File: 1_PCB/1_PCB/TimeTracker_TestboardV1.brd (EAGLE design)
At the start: 102.5 x 80 mm, 24 parts, among them IC1 7805DT, IC2 7805DT, J1 2908-05WB-MG, U1 WS2812B, U2 WS2812B, U3 WS2812B, U4 WS2812B, U5 SMTM1225, Y1 FX135A-327

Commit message: Humidity and Temp Sensor
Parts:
- added C5: (no value), rcl:C0805
- added HM1: SI7021-A20, SamacSys_Parts:SON100P300X300X80-7N
- added R1, R2: 10k, rcl:R0805
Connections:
- new net EP: HM1.7
- new net N$18: HM1.6, R2.1
- new net SDA: HM1.1, R1.1
- net 3V3: now also C5.1, HM1.5, R1.2, R2.2
- net GND: now also C5.2, HM1.2
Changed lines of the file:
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@@
 <attribute name="VALUE" x="-5.426" y="-20.147" size="1.27" layer="27" align="center"/>
+</element>
+<element name="HM1" library="SamacSys_Parts" package="SON100P300X300X80-7N" value="SI7021-A20" x="77.47" y="6.35" smashed="yes">
+<attribute name="DESCRIPTION" value="I2C HUMIDITY AND TEMPERATURE SENSOR" x="77.47" y="6.35" size="1.778" layer="27" display="off"/>
+<attribute name="HEIGHT" value="0.8mm" x="77.47" y="6.35" size="1.778" layer="27" display="off"/>
+<attribute name="MANUFACTURER_NAME" value="Silicon Labs" x="77.47" y="6.35" size="1.778" layer="27" display="off"/>
+<attribute name="MANUFACTURER_PART_NUMBER" value="Si7021-A20" x="77.47" y="6.35" size="1.778" layer="27" display="off"/>
+<attribute name="MOUSER_PART_NUMBER" value="" x="77.47" y="6.35" size="1.778" layer="27" display="off"/>
+<attribute name="MOUSER_PRICE-STOCK" value="" x="77.47" y="6.35" size="1.778" layer="27" display="off"/>
+<attribute name="NAME" x="88.9" y="3.81" size="1.27" layer="25" align="center"/>
+<attribute name="RS_PART_NUMBER" value="" x="77.47" y="6.35" size="1.778" layer="27" display="off"/>
+<attribute name="RS_PRICE-STOCK" value="" x="77.47" y="6.35" size="1.778" layer="27" display="off"/>
+<attribute name="VALUE" x="90.17" y="5.08" size="1.27" layer="27" align="center"/>
+</element>
+<element name="C5" library="rcl" library_urn="urn:adsk.eagle:library:334" package="C0805" package3d_urn="urn:adsk.eagle:package:23617/2" value="" x="-13.97" y="-33.02" smashed="yes">
+<attribute name="NAME" x="-15.24" y="-31.75" size="1.27" layer="25"/>
+<attribute name="SPICEPREFIX" value="C" x="-13.97" y="-33.02" size="1.778" layer="27" display="off"/>
+<attribute name="VALUE" x="-15.24" y="-35.56" size="1.27" layer="27"/>
+</element>
+<element name="R1" library="rcl" library_urn="urn:adsk.eagle:library:334" package="R0805" package3d_urn="urn:adsk.eagle:package:23553/2" value="10k" x="-13.97" y="-38.1" smashed="yes">
+<attribute name="NAME" x="-14.605" y="-36.83" size="1.27" layer="25"/>
+<attribute name="SPICEPREFIX" value="R" x="-13.97" y="-38.1" size="1.778" layer="27" display="off"/>
+<attribute name="VALUE" x="-14.605" y="-40.64" size="1.27" layer="27"/>
+</element>
+<element name="R2" library="rcl" library_urn="urn:adsk.eagle:library:334" package="R0805" package3d_urn="urn:adsk.eagle:package:23553/2" value="10k" x="-13.97" y="-44.45" smashed="yes">
+<attribute name="NAME" x="-14.605" y="-43.18" size="1.27" layer="25"/>
+<attribute name="SPICEPREFIX" value="R" x="-13.97" y="-44.45" size="1.778" layer="27" display="off"/>
+<attribute name="VALUE" x="-14.605" y="-46.99" size="1.27" layer="27"/>
 </element>
 </elements>
@@
 <contactref element="J1" pad="4"/>
 <contactref element="U$2" pad="8"/>
+<contactref element="HM1" pad="5"/>
+<contactref element="C5" pad="1"/>
+<contactref element="R1" pad="2"/>
+<contactref element="R2" pad="2"/>
 <wire x1="25.14" y1="67.59" x2="72.39" y2="69.85" width="0" layer="19" extent="1-1"/>
 <wire x1="25.4" y1="64.45" x2="25.14" y2="67.59" width="0" layer="19" extent="1-1"/>
 <wire x1="23.7" y1="50.505" x2="25.4" y2="64.45" width="0" layer="19" extent="1-1"/>
 <wire x1="10.92" y1="32.93" x2="23.7" y2="50.505" width="0" layer="19" extent="1-1"/>
+<wire x1="78.92" y1="6.35" x2="72.39" y2="69.85" width="0" layer="19" extent="1-1"/>
+<wire x1="-14.92" y1="-33.02" x2="10.92" y2="32.93" width="0" layer="19" extent="1-1"/>
+<wire x1="-13.02" y1="-38.1" x2="-14.92" y2="-33.02" width="0" layer="19" extent="1-1"/>
+<wire x1="-13.02" y1="-44.45" x2="-13.02" y2="-38.1" width="0" layer="19" extent="1-1"/>
 </signal>
 <signal name="GND">
@@
 <contactref element="LED_12V1" pad="C"/>
 <contactref element="U5" pad="2"/>
+<contactref element="HM1" pad="2"/>
+<contactref element="C5" pad="2"/>
 <wire x1="54.61" y1="29.21" x2="77.47" y2="69.85" width="0" layer="19" extent="1-1"/>
 <wire x1="39.37" y1="24.13" x2="54.61" y2="29.21" width="0" layer="19" extent="1-1"/>
@@
 <wire x1="22.86" y1="74.89" x2="20.574" y2="63.439" width="0" layer="19" extent="1-1"/>
 <wire x1="-5.08" y1="-20.32" x2="26.633" y2="9.22" width="0" layer="19" extent="1-1"/>
+<wire x1="76.02" y1="6.35" x2="-5.08" y2="-20.32" width="0" layer="19" extent="1-1"/>
+<wire x1="-13.02" y1="-33.02" x2="76.02" y2="6.35" width="0" layer="19" extent="1-1"/>
 </signal>
 <signal name="RFIDRESET">
@@
 <wire x1="-13.13" y1="-20.32" x2="19.48" y2="49.205" width="0" layer="19" extent="1-1"/>
 </signal>
+<signal name="EP">
+<contactref element="HM1" pad="7"/>
+</signal>
+<signal name="SDA">
+<contactref element="HM1" pad="1"/>
+<contactref element="R1" pad="1"/>
+<wire x1="-14.92" y1="-38.1" x2="76.02" y2="7.35" width="0" layer="19" extent="1-1"/>
+</signal>
+<signal name="N$18">
+<contactref element="HM1" pad="6"/>
+<contactref element="R2" pad="1"/>
+<wire x1="-14.92" y1="-44.45" x2="78.92" y2="7.35" width="0" layer="19" extent="1-1"/>
+</signal>
 </signals>

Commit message: Nico addition and modifications
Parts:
- removed J1: 2908-05WB-MG, 2908-05WB-MG:3M_2908-05WB-MG
- added JP6: USD_CONNECTOR, SparkFun-Connectors:MICRO-SD-SOCKET-PP
- added R6, R7, R8, R9: 100k, rcl:R0805
- moved U5 105.1 mm to (44.5, 72.4)
- moved Y1 99.9 mm to (55.9, 62.2), turned to 180 degrees
- moved U$2 39.8 mm to (57.1, 67.3), turned to 90 degrees
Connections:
- removed net N$4: J1.8
- removed net N$6: J1.1
- removed net N$7: J1.2
- removed net N$8: J1.3
- new net !CS_3V3: JP6.CS, R9.1
- new net CD: JP6.CD2
- new net CDSDSD: JP6.CD1, R8.1
- new net RSV@1: JP6.RSV1, R6.1
- new net RSV@2: JP6.RSV2, R7.1
- net 3V3: now also JP6.VCC, R6.2, R7.2, R9.2; no longer J1.4
- net 5V: now also R8.2
- net GND: now also JP6.GND, JP6.GND1, JP6.GND3; no longer J1.6
- net N$16: now also U5.3
- net SPIMISO: now also JP6.DO
- net SPIMOSI: now also JP6.DI; no longer J1.7
- net SPISCK: now also JP6.SCLK; no longer J1.5
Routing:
- net N$16: track 0.00 -> 36.6 mm
- net N$14: track 0.00 -> 3.61 mm
- net N$15: track 0.00 -> 3.10 mm

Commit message: Nico
Update PCB
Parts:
- added C6: 0.1uF, SparkFun-Capacitors:0603-CAP
- added C7, C9: 0.1u, rcl:C0805
- added C8: (no value), rcl:C0805
- added R10, R11, R12, R13, R4, R5: 10K, rcl:R0805
- added SJ4, SJ5: (no value), SparkFun-Passives:PAD-JUMPER-3-2OF3_NC_BY_TRACE_YES_SILK_FULL_BOX
- added U6: SX1509, SparkFun-DigitalIC:QFN-28
- moved R8 155.7 mm to (1.58, 19.8), turned to 180 degrees
- moved R7 132.9 mm to (1.71, 9.65), turned to 180 degrees
- moved R2 125.6 mm to (96.5, 15.2)
- moved C5 119.1 mm to (96.5, 11.4)
- moved R6 112.6 mm to (1.71, 2.03), turned to 180 degrees
- moved R1 111.3 mm to (86.4, 10.2), turned to 270 degrees
- moved R9 103.8 mm to (1.71, 5.97), turned to 180 degrees
- moved HM1 15.5 mm to (92.7, 8.89)
- moved JP5 14.8 mm to (30.5, 31.8)
- moved C2 0.92 mm to (25.1, 64.4)
- moved C4 0.28 mm to (7.87, 66.2)
- renumbered IC1 to LD1117DT33TR
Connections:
- removed net !CS_3V3: JP6.CS, R9.1
- removed net CD: JP6.CD2
- removed net N$18: HM1.6, R2.1
- removed net RFIDCS: JP1.1, JP3.2
- removed net RFIDRESET: JP1.7, JP2.2
- removed net SDA: HM1.1, R1.1
- new net !INT: R10.1, U6.9
- new net !RESET: R4.1, U6.23
- new net !SD_CS: JP6.CS, R9.1, U6.27
- new net 10: U6.15
- new net 11: U6.16
- new net 12: U6.19
- new net 13: U6.20
- new net 14: U6.21
- new net 15: U6.22
- new net 4: U6.5
- new net 5: U6.6
- new net 6: U6.7
- new net 7: U6.8
- new net 8: U6.13
- new net 9: U6.14
- new net ADDR0: SJ4.2, U6.26
- new net ADDR1: SJ5.2, U6.10
- new net I2CSCL: HM1.6, R12.1, R2.1, U$1.A5, U$2.6, U6.25
- new net I2CSDA: HM1.1, R1.1, R13.1, U$1.A4, U$2.5, U6.24
- new net LED_DIN: U$1.D2, U4.4
- new net N$6: R11.1, SJ5.1
- new net N$8: R5.1, SJ4.1
- new net OSCIO: U6.11
- new net RFID_CS: JP1.1, JP3.2, U6.1
- new net RFID_RESET: JP1.7, JP2.2, U6.2
- new net SD_CD: JP6.CD2, U6.28
- net 3V3: now also C6.1, C7.1, C8.1, C9.1, R10.2, R11.2, R12.2, R13.2, R4.2, R5.2, R8.2, U6.12, U6.18, U6.4
- net 5V: no longer R8.2
- net GND: now also C6.2, C7.2, C8.2, C9.2, SJ4.3, SJ5.3, U6.17, U6.29, U6.3
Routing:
- net 3V3: track 0.00 -> 329.3 mm
- net I2CSCL: track 0.00 -> 170.2 mm, vias 0 -> 6
- net I2CSDA: track 0.00 -> 153.6 mm, vias 0 -> 5
- net SPISCK: track 0.00 -> 125.3 mm, vias 0 -> 2
- net SPIMOSI: track 0.00 -> 124.1 mm, vias 0 -> 1
- net SPIMISO: track 0.00 -> 123.5 mm, vias 0 -> 1
- net RFID_RESET: track 0.00 -> 87.7 mm, vias 0 -> 1
- net SD_CD: track 0.00 -> 83.5 mm, vias 0 -> 2
- net RFID_CS: track 0.00 -> 76.2 mm
- net 5V: track 27.0 -> 97.5 mm, vias 2 -> 3
- net LED_DIN: track 0.00 -> 37.9 mm, vias 0 -> 1
- net ADDR1: track 0.00 -> 32.2 mm, vias 0 -> 2
- net N$12: track 2.54 -> 21.3 mm
- net RSV@1: track 0.00 -> 15.3 mm
- net N$1: track 23.9 -> 37.9 mm
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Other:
- outline, holes or cut-outs redrawn

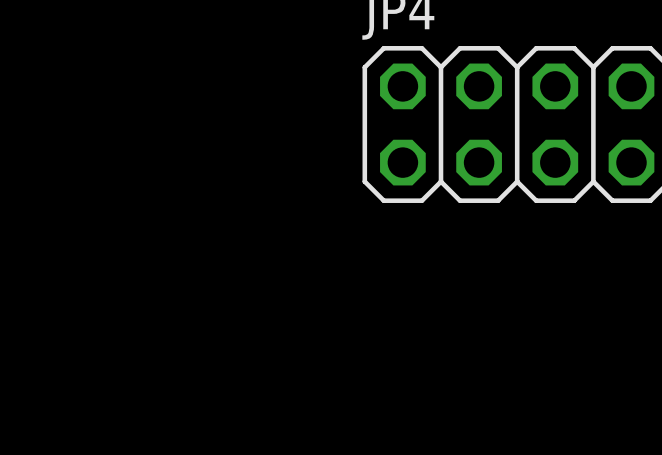
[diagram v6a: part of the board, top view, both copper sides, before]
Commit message: Added a new Voltage Regulator
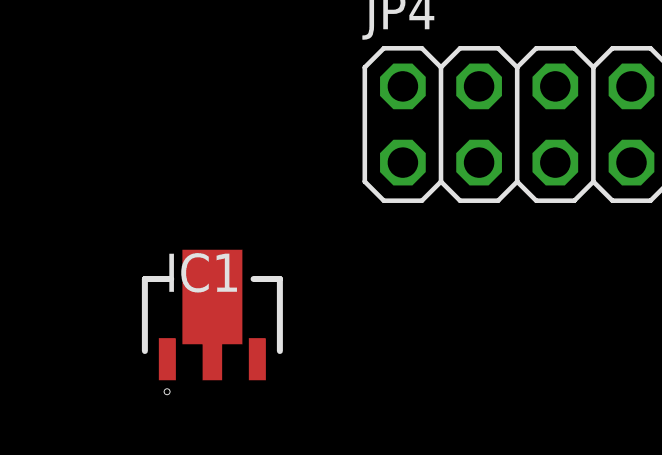
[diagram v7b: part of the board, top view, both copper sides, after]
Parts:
- added IC1: L78L33ABUTR, SamacSys_Parts:ST-SOT-89
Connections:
- new net GND_(TAB): IC1.4
- net GND: now also IC1.2
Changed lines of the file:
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@@
 <?xml version="1.0" encoding="utf-8"?>
 <!DOCTYPE eagle SYSTEM "eagle.dtd">
-<eagle version="9.3.0">
+<eagle version="9.2.2">
 <drawing>
 <settings>
@@
 <attribute name="VALUE" x="57.15" y="73.66" size="1.27" layer="27"/>
 </element>
+<element name="IC1" library="SamacSys_Parts" package="ST-SOT-89" value="L78L33ABUTR" x="-16.51" y="-13.97" smashed="yes">
+<attribute name="ALLIED_NUMBER" value="70390115" x="-16.51" y="-13.97" size="1.778" layer="27" display="off"/>
+<attribute name="ALLIED_PRICE-STOCK" value="http://www.alliedelec.com/stmicroelectronics-l78l33abutr/70390115/" x="-16.51" y="-13.97" size="1.778" layer="27" display="off"/>
+<attribute name="DESCRIPTION" value="L78L33ABUTR, Voltage Regulator, 0.1A 3.3 V, 4-Pin SOT-89" x="-16.51" y="-13.97" size="1.778" layer="27" display="off"/>
+<attribute name="HEIGHT" value="mm" x="-16.51" y="-13.97" size="1.778" layer="27" display="off"/>
+<attribute name="MANUFACTURER_NAME" value="STMicroelectronics" x="-16.51" y="-13.97" size="1.778" layer="27" display="off"/>
+<attribute name="MANUFACTURER_PART_NUMBER" value="L78L33ABUTR" x="-16.51" y="-13.97" size="1.778" layer="27" display="off"/>
+<attribute name="MOUSER_PART_NUMBER" value="511-L78L33ABU-TR" x="-16.51" y="-13.97" size="1.778" layer="27" display="off"/>
+<attribute name="MOUSER_PRICE-STOCK" value="https://www.mouser.com/Search/Refine.aspx?Keyword=511-L78L33ABU-TR" x="-16.51" y="-13.97" size="1.778" layer="27" display="off"/>
+<attribute name="NAME" x="-16.823" y="-12.563" size="1.27" layer="25" align="center"/>
+<attribute name="RS_PART_NUMBER" value="6869464P" x="-16.51" y="-13.97" size="1.778" layer="27" display="off"/>
+<attribute name="RS_PRICE-STOCK" value="http://uk.rs-online.com/web/p/products/6869464P" x="-16.51" y="-13.97" size="1.778" layer="27" display="off"/>
+<attribute name="VALUE" x="-16.823" y="-12.563" size="1.27" layer="27" align="center"/>
+</element>
 </elements>
 <signals>
@@
 <wire x1="64.9553125" y1="11.1014" x2="64.6267125" y2="11.43" width="0.1524" layer="1"/>
 <contactref element="C8" pad="2"/>
+<contactref element="IC1" pad="2"/>
+<wire x1="59.37" y1="76.2" x2="77.47" y2="69.85" width="0" layer="19" extent="1-1"/>
+<wire x1="58.125" y1="65.2" x2="59.37" y2="76.2" width="0" layer="19" extent="1-1"/>
+<wire x1="44.45" y1="72.39" x2="59.37" y2="76.2" width="0" layer="19" extent="1-1"/>
+<wire x1="25.146" y1="63.439" x2="44.45" y2="72.39" width="0" layer="19" extent="1-1"/>
+<wire x1="20.574" y1="63.439" x2="25.146" y2="63.439" width="0" layer="19" extent="1-1"/>
+<wire x1="12.446" y1="67.117" x2="20.574" y2="63.439" width="0" layer="19" extent="1-1"/>
+<wire x1="7.874" y1="67.117" x2="12.446" y2="67.117" width="0" layer="19" extent="1-1"/>
+<wire x1="5.89" y1="74.93" x2="7.874" y2="67.117" width="0" layer="19" extent="1-1"/>
+<wire x1="1.27" y1="59.91" x2="7.874" y2="67.117" width="0" layer="19" extent="1-1"/>
+<wire x1="10.16" y1="55.92" x2="1.27" y2="59.91" width="0" layer="19" extent="1-1"/>
+<wire x1="22.86" y1="74.89" x2="25.146" y2="63.439" width="0" layer="19" extent="1-1"/>
+<wire x1="54.61" y1="29.21" x2="58.125" y2="65.2" width="0" layer="19" extent="1-1"/>
+<wire x1="64.77" y1="18.73" x2="54.61" y2="29.21" width="0" layer="19" extent="1-1"/>
+<wire x1="64.6267125" y1="11.43" x2="64.77" y2="18.73" width="0" layer="19" extent="1-1"/>
+<wire x1="71.335" y1="12.319" x2="65.475" y2="11.03" width="0" layer="19" extent="1-1"/>
+<wire x1="73.2028" y1="6.35" x2="71.335" y2="12.319" width="0" layer="19" extent="1-1"/>
+<wire x1="79.5528" y1="6.35" x2="73.2028" y2="6.35" width="0" layer="19" extent="1-1"/>
+<wire x1="54.93" y1="10.16" x2="61.525" y2="11.83" width="0" layer="19" extent="1-1"/>
+<wire x1="91.26" y1="8.89" x2="79.5528" y2="6.35" width="0" layer="19" extent="1-1"/>
+<wire x1="97.47" y1="11.43" x2="91.26" y2="8.89" width="0" layer="19" extent="1-1"/>
+<wire x1="39.37" y1="24.13" x2="54.61" y2="29.21" width="0" layer="19" extent="1-1"/>
+<wire x1="34.6202" y1="22.1234" x2="39.37" y2="24.13" width="0" layer="19" extent="1-1"/>
+<wire x1="28.1178" y1="22.1234" x2="34.6202" y2="22.1234" width="0" layer="19" extent="1-1"/>
+<wire x1="35.523" y1="15.57" x2="34.6202" y2="22.1234" width="0" layer="19" extent="1-1"/>
+<wire x1="35.523" y1="9.22" x2="35.523" y2="15.57" width="0" layer="19" extent="1-1"/>
+<wire x1="26.633" y1="15.57" x2="28.1178" y2="22.1234" width="0" layer="19" extent="1-1"/>
+<wire x1="26.633" y1="9.22" x2="26.633" y2="15.57" width="0" layer="19" extent="1-1"/>
+<wire x1="18.68" y1="5.77" x2="26.633" y2="9.22" width="0" layer="19" extent="1-1"/>
+<wire x1="8.52" y1="9.42" x2="18.68" y2="5.77" width="0" layer="19" extent="1-1"/>
 <wire x1="5.53" y1="6.77" x2="8.52" y2="9.42" width="0" layer="19" extent="1-1"/>
-<wire x1="26.633" y1="9.22" x2="18.68" y2="5.77" width="0" layer="19" extent="1-1"/>
-<wire x1="91.26" y1="8.89" x2="97.47" y2="11.43" width="0" layer="19" extent="1-1"/>
+<wire x1="-16.51" y1="-15.545" x2="5.53" y2="6.77" width="0" layer="19" extent="1-1"/>
 </signal>
 <signal name="RFID_RESET">
@@
 <wire x1="38.989" y1="6.35" x2="40.259" y2="7.62" width="0.1524" layer="1"/>
 </signal>
+<signal name="GND_(TAB)">
+<contactref element="IC1" pad="4"/>
+</signal>
 </signals>

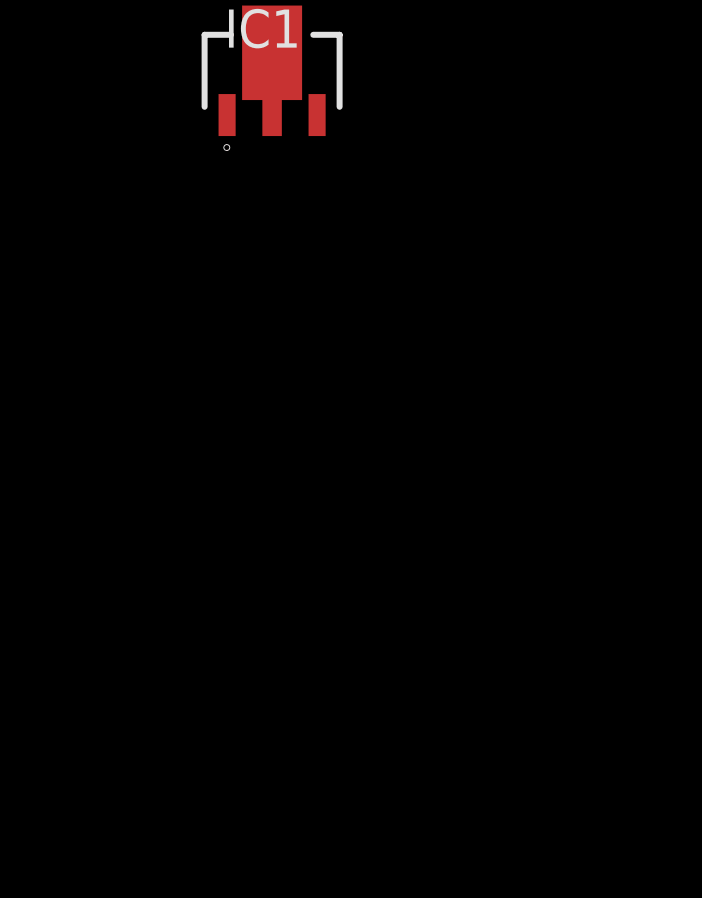
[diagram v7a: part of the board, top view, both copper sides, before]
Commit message: I/O Expander changed
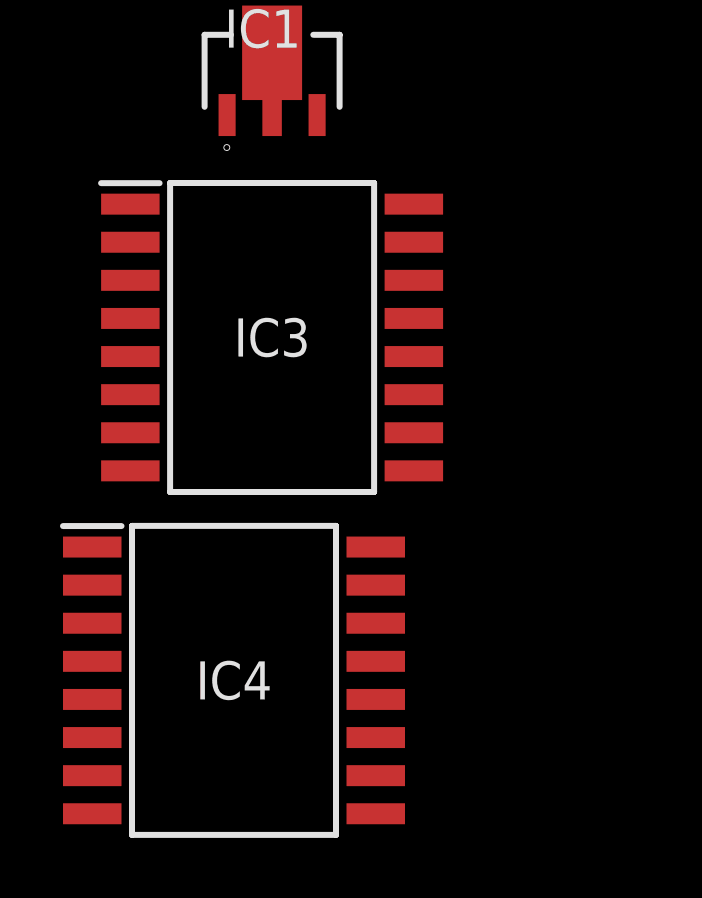
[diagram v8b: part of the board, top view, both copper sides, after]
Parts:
- added IC3, IC4: PCF8574T_3,518, SamacSys_Parts:SOIC127P1032X265-16N
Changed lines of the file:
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@@
 <attribute name="VALUE" x="-16.823" y="-12.563" size="1.27" layer="27" align="center"/>
+</element>
+<element name="IC3" library="SamacSys_Parts" package="SOIC127P1032X265-16N" value="PCF8574T_3,518" x="-16.51" y="-22.86" smashed="yes">
+<attribute name="DESCRIPTION" value="NXP - PCF8574T/3,518 - IC, I/O EXPANDER, 8BIT, SOIC16" x="-16.51" y="-22.86" size="1.778" layer="27" display="off"/>
+<attribute name="HEIGHT" value="2.65mm" x="-16.51" y="-22.86" size="1.778" layer="27" display="off"/>
+<attribute name="MANUFACTURER_NAME" value="Nexperia" x="-16.51" y="-22.86" size="1.778" layer="27" display="off"/>
+<attribute name="MANUFACTURER_PART_NUMBER" value="PCF8574T/3,518" x="-16.51" y="-22.86" size="1.778" layer="27" display="off"/>
+<attribute name="MOUSER_PART_NUMBER" value="771-PCF8574TD-T" x="-16.51" y="-22.86" size="1.778" layer="27" display="off"/>
+<attribute name="MOUSER_PRICE-STOCK" value="https://www.mouser.com/Search/Refine.aspx?Keyword=771-PCF8574TD-T" x="-16.51" y="-22.86" size="1.778" layer="27" display="off"/>
+<attribute name="NAME" x="-16.51" y="-22.86" size="1.27" layer="25" align="center"/>
+<attribute name="RS_PART_NUMBER" value="" x="-16.51" y="-22.86" size="1.778" layer="27" display="off"/>
+<attribute name="RS_PRICE-STOCK" value="" x="-16.51" y="-22.86" size="1.778" layer="27" display="off"/>
+<attribute name="VALUE" x="-16.51" y="-22.86" size="1.27" layer="27" align="center"/>
+</element>
+<element name="IC4" library="SamacSys_Parts" package="SOIC127P1032X265-16N" value="PCF8574T_3,518" x="-17.78" y="-34.29" smashed="yes">
+<attribute name="DESCRIPTION" value="NXP - PCF8574T/3,518 - IC, I/O EXPANDER, 8BIT, SOIC16" x="-17.78" y="-34.29" size="1.778" layer="27" display="off"/>
+<attribute name="HEIGHT" value="2.65mm" x="-17.78" y="-34.29" size="1.778" layer="27" display="off"/>
+<attribute name="MANUFACTURER_NAME" value="Nexperia" x="-17.78" y="-34.29" size="1.778" layer="27" display="off"/>
+<attribute name="MANUFACTURER_PART_NUMBER" value="PCF8574T/3,518" x="-17.78" y="-34.29" size="1.778" layer="27" display="off"/>
+<attribute name="MOUSER_PART_NUMBER" value="771-PCF8574TD-T" x="-17.78" y="-34.29" size="1.778" layer="27" display="off"/>
+<attribute name="MOUSER_PRICE-STOCK" value="https://www.mouser.com/Search/Refine.aspx?Keyword=771-PCF8574TD-T" x="-17.78" y="-34.29" size="1.778" layer="27" display="off"/>
+<attribute name="NAME" x="-17.78" y="-34.29" size="1.27" layer="25" align="center"/>
+<attribute name="RS_PART_NUMBER" value="" x="-17.78" y="-34.29" size="1.778" layer="27" display="off"/>
+<attribute name="RS_PRICE-STOCK" value="" x="-17.78" y="-34.29" size="1.778" layer="27" display="off"/>
+<attribute name="VALUE" x="-17.78" y="-34.29" size="1.27" layer="27" align="center"/>
 </element>
 </elements>
